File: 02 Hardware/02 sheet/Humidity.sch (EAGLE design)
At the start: 19 parts, among them IC1 IRM-03, IC2 ESP8266, J1 AC 230V, J2 Fan, J3 DHT22_OUT, J4 DHT22_IN, K1 351, Q1 TRANSISTOR-NPN_BC817SMD

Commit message: Signed-off-by: Joe G <grabow@amesys.de>
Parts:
- J3: value DHT22_OUT -> AM2302_OUT
- J4: value DHT22_IN -> AM2302_IN
- Q1: value TRANSISTOR-NPN_BC817SMD -> BC817
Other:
- note added: "L"
- note added: "N"
- note added: "PE"

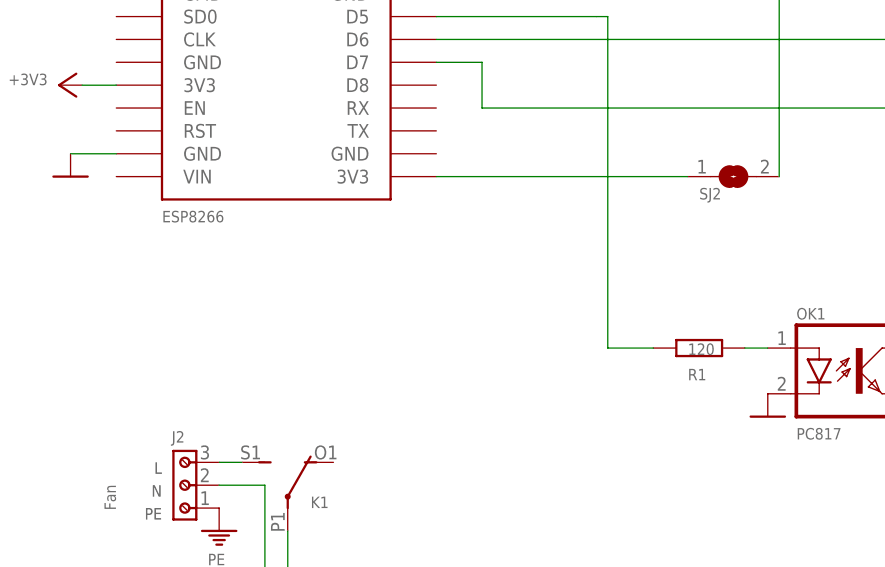
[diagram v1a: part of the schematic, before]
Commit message: with AMICA Package
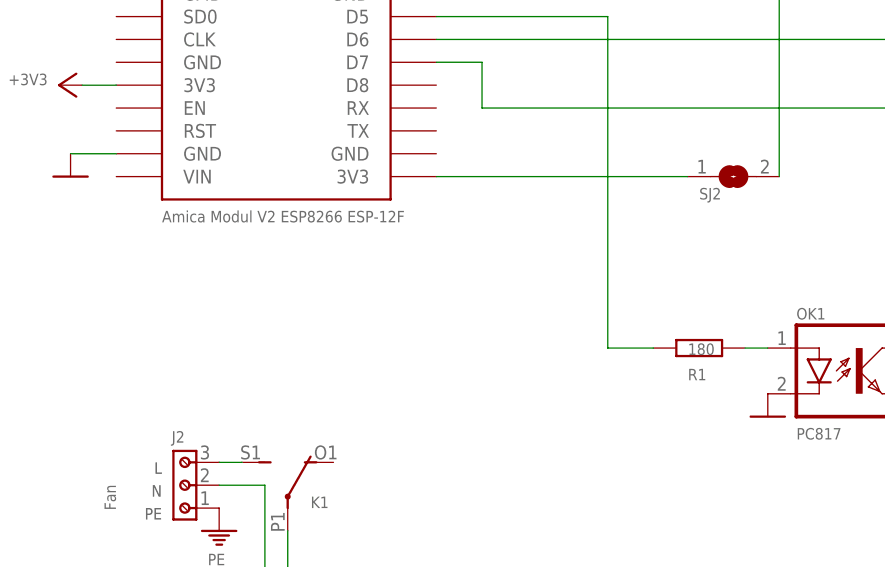
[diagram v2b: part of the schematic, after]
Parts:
- IC2: value ESP8266 -> Amica Modul V2 ESP8266 ESP-12F
- R1: value 120 -> 180
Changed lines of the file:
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@@
 <setting verticaltext="up"/>
 </settings>
-<grid distance="0.05" unitdist="inch" unit="inch" style="lines" multiple="1" display="no" altdistance="0.01" altunitdist="inch" altunit="inch"/>
+<grid distance="0.1" unitdist="inch" unit="inch" style="lines" multiple="1" display="no" altdistance="0.01" altunitdist="inch" altunit="inch"/>
 <layers>
 <layer number="1" name="Top" color="4" fill="1" visible="no" active="no"/>
@@
 <part name="IC1" library="meanwell" deviceset="IRM-03" device=""/>
 <part name="K1" library="relay" library_urn="urn:adsk.eagle:library:339" deviceset="351" device="" package3d_urn="urn:adsk.eagle:package:24300/1"/>
-<part name="R1" library="rcl" library_urn="urn:adsk.eagle:library:334" deviceset="R-EU_" device="R1206" package3d_urn="urn:adsk.eagle:package:23540/2" value="120"/>
+<part name="R1" library="rcl" library_urn="urn:adsk.eagle:library:334" deviceset="R-EU_" device="R1206" package3d_urn="urn:adsk.eagle:package:23540/2" value="180"/>
 <part name="R2" library="rcl" library_urn="urn:adsk.eagle:library:334" deviceset="R-EU_" device="M1206" package3d_urn="urn:adsk.eagle:package:23566/2" value="1k"/>
 <part name="GND3" library="supply1" library_urn="urn:adsk.eagle:library:371" deviceset="GND" device=""/>
@@
 <part name="C2" library="rcl" library_urn="urn:adsk.eagle:library:334" deviceset="CPOL-EU" device="SMCC" package3d_urn="urn:adsk.eagle:package:25921/2" value="100µF"/>
 <part name="P+4" library="supply1" library_urn="urn:adsk.eagle:library:371" deviceset="+5V" device=""/>
-<part name="IC2" library="ESP12E_DEVKIT" deviceset="ESP12E_DEVKIT" device="" value="ESP8266"/>
+<part name="IC2" library="ESP12E_DEVKIT" deviceset="ESP12E_DEVKIT" device="" value="Amica Modul V2 ESP8266 ESP-12F"/>
 <part name="+3V2" library="supply1" library_urn="urn:adsk.eagle:library:371" deviceset="+3V3" device=""/>
 <part name="GND7" library="supply1" library_urn="urn:adsk.eagle:library:371" deviceset="GND" device=""/>

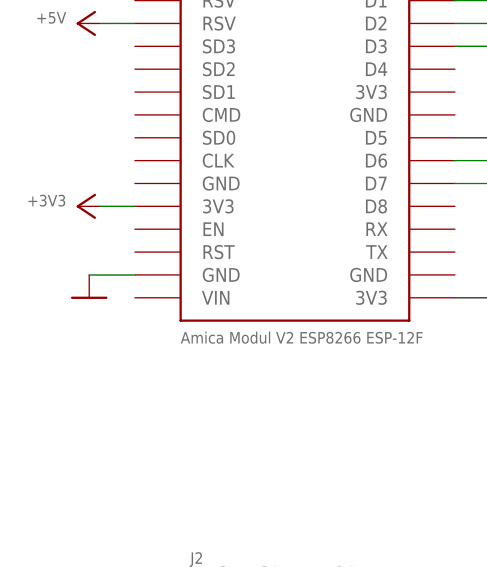
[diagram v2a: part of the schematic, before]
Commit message: Dugfix Boarddesign
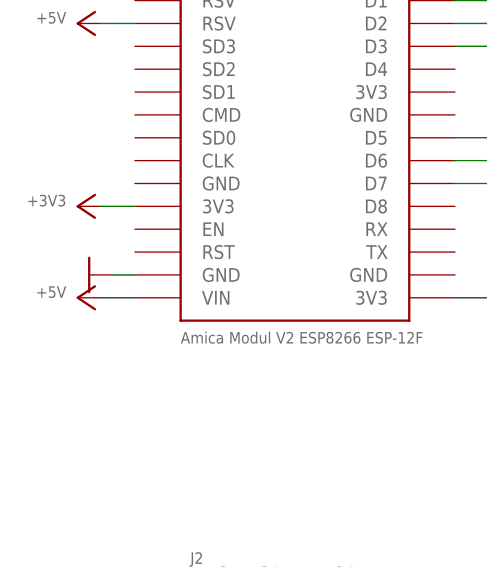
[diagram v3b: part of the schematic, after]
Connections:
- net +5V: now also IC2.VIN
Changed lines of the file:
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@@
 <setting verticaltext="up"/>
 </settings>
-<grid distance="0.1" unitdist="inch" unit="inch" style="lines" multiple="1" display="no" altdistance="0.01" altunitdist="inch" altunit="inch"/>
+<grid distance="0.05" unitdist="inch" unit="inch" style="lines" multiple="1" display="no" altdistance="0.01" altunitdist="inch" altunit="inch"/>
 <layers>
 <layer number="1" name="Top" color="4" fill="1" visible="no" active="no"/>
@@
 <part name="PE1" library="supply1" library_urn="urn:adsk.eagle:library:371" deviceset="PE" device=""/>
 <part name="PE2" library="supply1" library_urn="urn:adsk.eagle:library:371" deviceset="PE" device=""/>
+<part name="P+6" library="supply1" library_urn="urn:adsk.eagle:library:371" deviceset="+5V" device=""/>
 </parts>
 <sheets>
@@
 <attribute name="VALUE" x="66.04" y="110.49" size="1.27" layer="96" rot="R180"/>
 </instance>
-<instance part="GND7" gate="1" x="68.58" y="99.06" smashed="yes"/>
+<instance part="GND7" gate="1" x="68.58" y="101.6" smashed="yes" rot="R270"/>
 <instance part="R3" gate="G$1" x="170.18" y="121.92" smashed="yes" rot="R270">
 <attribute name="NAME" x="171.6786" y="123.19" size="1.27" layer="95" rot="R270"/>
@@
 <instance part="PE2" gate="M" x="85.09" y="39.37" smashed="yes">
 <attribute name="VALUE" x="83.82" y="35.56" size="1.27" layer="96"/>
+</instance>
+<instance part="P+6" gate="1" x="67.31" y="99.06" smashed="yes" rot="R90">
+<attribute name="VALUE" x="66.04" y="100.33" size="1.27" layer="96" rot="R180"/>
 </instance>
 </instances>
@@
 <pinref part="IC2" gate="G$1" pin="GND@1"/>
 <pinref part="GND7" gate="1" pin="GND"/>
-<wire x1="73.66" y1="101.6" x2="68.58" y2="101.6" width="0.1524" layer="91"/>
+<wire x1="73.66" y1="101.6" x2="71.12" y2="101.6" width="0.1524" layer="91"/>
 </segment>
 <segment>
@@
 <pinref part="SJ1" gate="1" pin="1"/>
 </segment>
-</net>
+<segment>
+<pinref part="P+6" gate="1" pin="+5V"/>
+<pinref part="IC2" gate="G$1" pin="VIN"/>
+<wire x1="69.85" y1="99.06" x2="73.66" y2="99.06" width="0.1524" layer="91"/>
+</segment>
+</net>

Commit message: Schaltung
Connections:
- net +5V: now also D1.C; no longer D1.A
- net N$8: now also D1.A; no longer D1.C
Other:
- moved on the sheet: D1
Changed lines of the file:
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@@
 <layer number="91" name="Nets" color="2" fill="1" visible="yes" active="yes"/>
 <layer number="92" name="Busses" color="1" fill="1" visible="yes" active="yes"/>
-<layer number="93" name="Pins" color="2" fill="1" visible="no" active="yes"/>
+<layer number="93" name="Pins" color="2" fill="1" visible="yes" active="yes"/>
 <layer number="94" name="Symbols" color="4" fill="1" visible="yes" active="yes"/>
 <layer number="95" name="Names" color="7" fill="1" visible="yes" active="yes"/>
@@
 </instance>
 <instance part="GND4" gate="1" x="173.99" y="67.31" smashed="yes"/>
-<instance part="D1" gate="G$1" x="181.61" y="85.09" smashed="yes" rot="R270">
-<attribute name="NAME" x="184.15" y="85.5726" size="1.27" layer="95"/>
-<attribute name="VALUE" x="184.15" y="81.5086" size="1.27" layer="96"/>
+<instance part="D1" gate="G$1" x="181.61" y="85.09" smashed="yes" rot="R90">
+<attribute name="NAME" x="179.07" y="84.6074" size="1.27" layer="95" rot="R180"/>
+<attribute name="VALUE" x="179.07" y="88.6714" size="1.27" layer="96" rot="R180"/>
 </instance>
 <instance part="P+3" gate="1" x="120.65" y="49.53" smashed="yes">
@@
 <wire x1="173.99" y1="90.17" x2="181.61" y2="90.17" width="0.1524" layer="91"/>
 <junction x="173.99" y="90.17"/>
-<pinref part="D1" gate="G$1" pin="A"/>
-<wire x1="181.61" y1="90.17" x2="181.61" y2="87.63" width="0.1524" layer="91"/>
+<pinref part="D1" gate="G$1" pin="C"/>
+<wire x1="181.61" y1="87.63" x2="181.61" y2="90.17" width="0.1524" layer="91"/>
 </segment>
 <segment>
@@
 <wire x1="173.99" y1="80.01" x2="181.61" y2="80.01" width="0.1524" layer="91"/>
 <junction x="173.99" y="80.01"/>
-<pinref part="D1" gate="G$1" pin="C"/>
-<wire x1="181.61" y1="80.01" x2="181.61" y2="82.55" width="0.1524" layer="91"/>
-</segment>
-</net>
+<pinref part="D1" gate="G$1" pin="A"/>
+<wire x1="181.61" y1="82.55" x2="181.61" y2="80.01" width="0.1524" layer="91"/>
+</segment>
+</net>
